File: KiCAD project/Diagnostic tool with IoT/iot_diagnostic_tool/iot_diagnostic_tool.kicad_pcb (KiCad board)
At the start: 4 copper layers, 50 x 50 mm, 113 parts, among them J2 USB, J3 693023010811, J5 Debug, J6 BOOT, J7 OBD, Q1 s8050, Q2 s8050, Q3 s8050, Q4 s8050, Q5 s8050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

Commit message: Update 07/03/23 - board layout done
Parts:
- removed D3, D4: LED, LED_SMD:LED_0402_1005Metric
- removed Q4, Q5: s8050, Package_TO_SOT_SMD:SOT-23
- removed R22, R26: 4k7, Resistor_SMD:R_0402_1005Metric
- removed R23, R27: 47k, Resistor_SMD:R_0402_1005Metric
- removed R24, R25: 2k2, Resistor_SMD:R_0402_1005Metric
- moved R14 32.0 mm to (147.0, 101.2)
- moved Q3 31.4 mm to (144.5, 100.4), turned to 0 degrees
- moved C25 31.1 mm to (142.1, 101.0)
- moved R15 29.9 mm to (145.1, 102.7), turned to 0 degrees
- moved R41 23.5 mm to (152.0, 83.9), turned to 180 degrees
- moved R43 22.3 mm to (144.8, 81.3), turned to 180 degrees
- moved R42 21.8 mm to (149.9, 83.9)
- moved Q7 18.7 mm to (150.8, 81.5), turned to 180 degrees
- moved Q6 16.0 mm to (147.7, 79.8)
- moved R40 13.8 mm to (150.9, 79.0), turned to 0 degrees
- moved R8 0.30 mm to (162.9, 99.3)
- moved R39 0.14 mm to (132.8, 77.8), turned to -90 degrees
- moved R38 0.08 mm to (140.6, 77.9), turned to -90 degrees
- moved D8 0.08 mm to (133.7, 117.7)
- turned R28 to 180 degrees
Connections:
- AE1 pad 1: Net-(AE1-A) -> ANT_MAIN
- AE1 pad 2: (no net) -> GND
- AE2 pad 1: Net-(AE2-A) -> ANT_GNSS
- AE2 pad 2: (no net) -> GND
- C1 pad 1: VDD -> +3V3
- C15 pad 1: VDD -> +3V3
- C16 pad 1: VDD -> +3V3
- C17 pad 1: VDD -> +3V3
- C18 pad 1: VDD -> +3V3
- C2 pad 1: VDD -> +3V3
- C21 pad 1: VBAT -> +3V3
- C22 pad 1: VBAT -> +3V3
- C23 pad 1: VBAT -> +3V3
- C24 pad 1: VBAT -> +3V3
- C28 pad 1: VDD -> +3V3
- C3 pad 1: VDD -> +3V3
- C39 pad 1: Net-(AE1-A) -> ANT_MAIN
- C4 pad 1: VDD -> +3V3
- C41 pad 1: Net-(AE2-A) -> ANT_GNSS
- C5 pad 1: VDD -> +3V3
- C6 pad 1: VDD -> +3V3
- C7 pad 1: VDD -> +3V3
- D11 pad 1: VBAT -> +3V3
- J2 pad 2: VDD -> +3V3
- J5 pad 1: VDD -> +3V3
- J6 pad 1: VDD -> +3V3
- L1 pad 2: VDD -> +3V3
- R12 pad 1: /car_comm/+12V_F -> /power_supply/+12V_F
- R16 pad 1: VBAT -> +3V3
- R2 pad 1: VDD -> +3V3
- R38 pad 2: Net-(AE1-A) -> ANT_MAIN
- R39 pad 2: Net-(AE2-A) -> ANT_GNSS
- R7 pad 1: /car_comm/+12V_F -> /power_supply/+12V_F
- R9 pad 1: /car_comm/+12V_F -> /power_supply/+12V_F
- U1 pad 1: VDD -> +3V3
- U1 pad 13: VDD -> +3V3
- U1 pad 19: VDD -> +3V3
- U1 pad 32: VDD -> +3V3
- U1 pad 48: VDD -> +3V3
- U1 pad 64: VDD -> +3V3
- U3 pad 3: VDD -> +3V3
- U4 pad 19: VBAT -> +3V3
- U4 pad 20: VBAT -> +3V3
- U4 pad 78: STATUS -> unconnected-(U4-STATUS-Pad78)
- U4 pad 79: NET_STATUS -> unconnected-(U4-NET_STATUS-Pad79)
- U6 pad 3: VDD -> +3V3
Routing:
- net NRST: track 9.75 -> 70.3 mm, vias 2 -> 0
- net +1V8: track 57.8 -> 97.7 mm
- net RESET_N: track 12.0 -> 45.9 mm, vias 2 -> 4
- net +3V3: track 0.00 -> 24.3 mm, vias 0 -> 22
- net VDD: track 21.0 -> 0.00 mm, vias 14 -> 0
- net IoT_PWR: track 1.48 -> 16.7 mm, vias 1 -> 2
- net GND: track 37.2 -> 22.2 mm, vias 57 -> 249
- net PON_TRIG: track 0.94 -> 12.2 mm
- net /power_supply/+12V_F: track 2.67 -> 11.3 mm, vias 0 -> 2
- net PON_TRIG_MCU: track 0.00 -> 7.67 mm, vias 0 -> 1
- net PWRKEY: track 5.71 -> 12.6 mm, vias 1 -> 0
- net ANT_MAIN: track 0.00 -> 6.68 mm
- net ANT_GNSS: track 0.00 -> 6.53 mm
- net Net-(Q6-G): track 0.00 -> 5.47 mm
- net Net-(Q3-B): track 0.00 -> 5.17 mm
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- added copper zone on F.Cu, net +3V3
- added copper zone on In2.Cu, net +3V3
- removed copper zone on F.Cu, net VBAT
- removed copper zone on F.Cu, net VDD

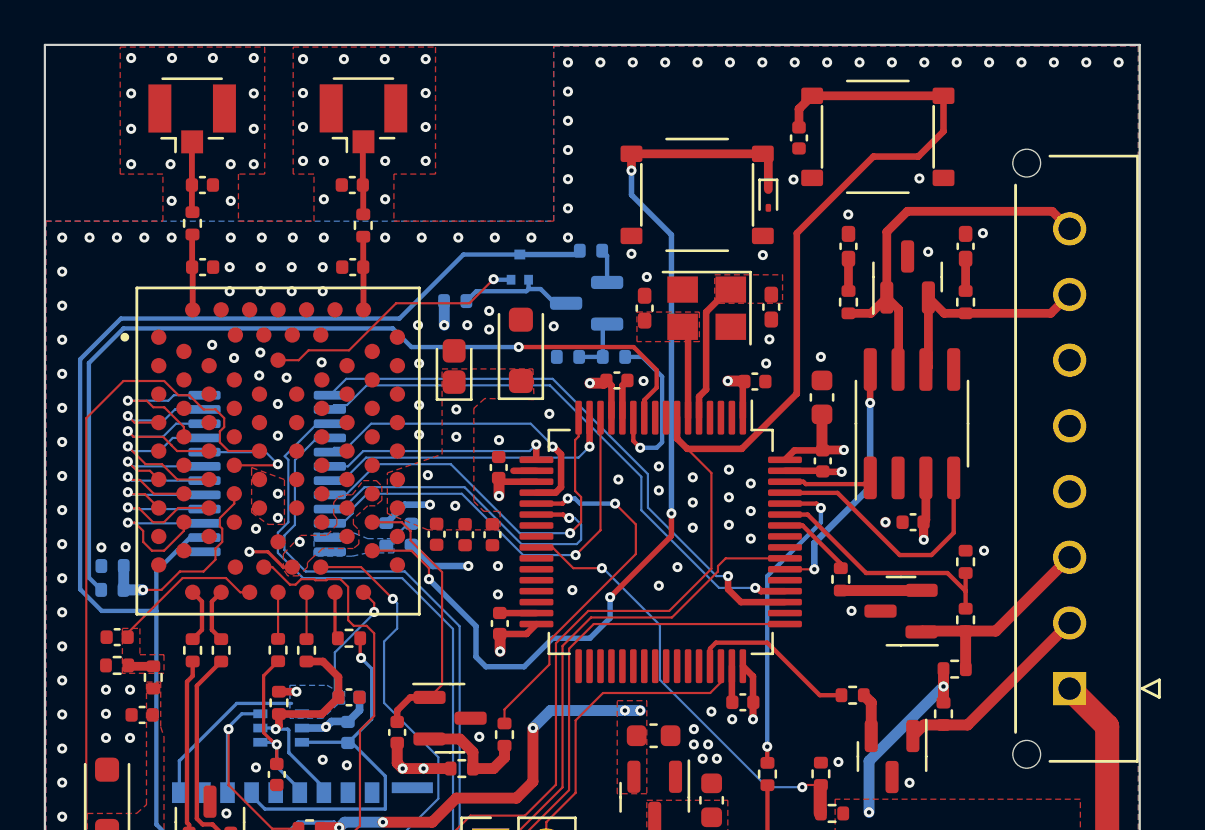
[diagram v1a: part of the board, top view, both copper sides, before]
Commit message: Update 13/03/23 - Board layout fixes
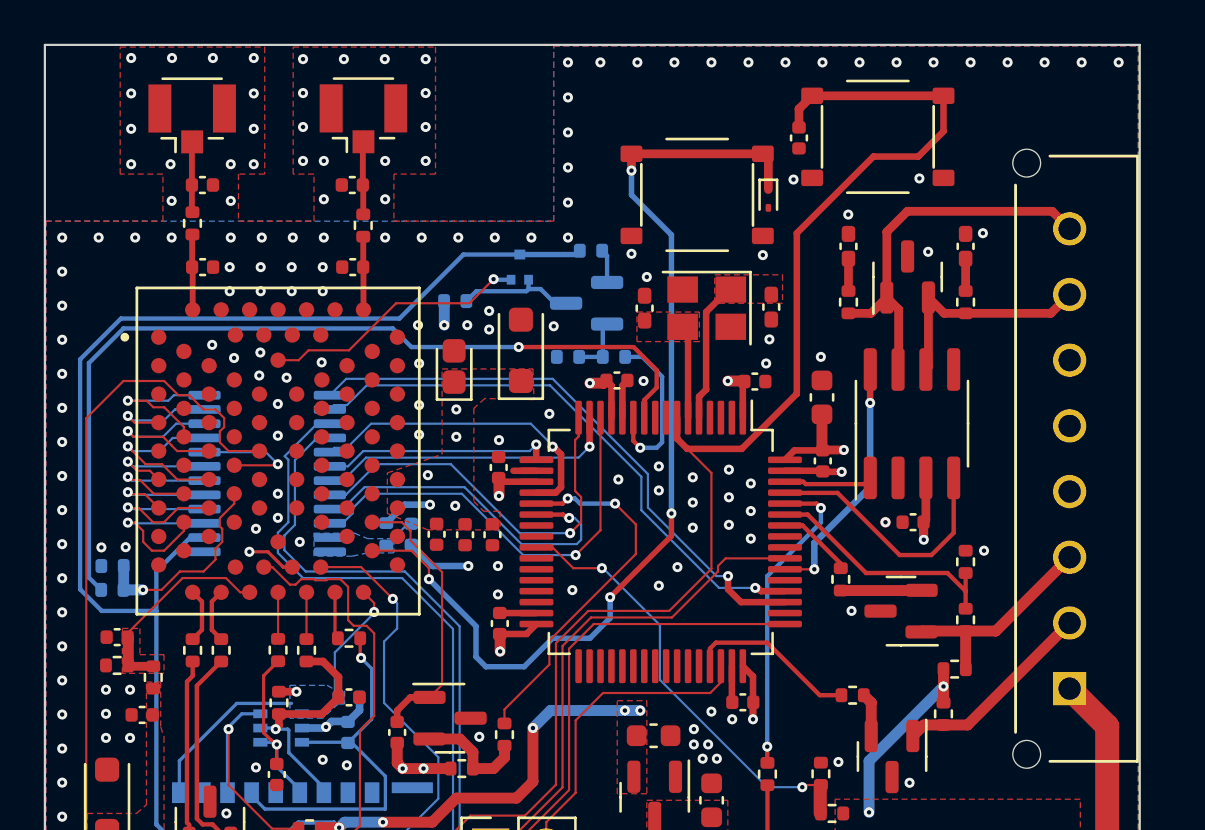
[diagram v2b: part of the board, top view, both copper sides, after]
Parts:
- turned R38 to 90 degrees
- turned R39 to 90 degrees
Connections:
- AE1 pad 1: ANT_MAIN -> /iot_module/antenna/ANT_M
- AE1 pad 2: GND -> (no net)
- AE2 pad 1: ANT_GNSS -> /iot_module/antenna/ANT_G
- AE2 pad 2: GND -> (no net)
- C33 pad 1: SIM_RST -> /iot_module/sim/SIM_RES
- C39 pad 1: ANT_MAIN -> /iot_module/antenna/ANT_M
- C41 pad 1: ANT_GNSS -> /iot_module/antenna/ANT_G
- D5 pad 3: SIM_RST -> /iot_module/sim/SIM_RES
- D7 pad 1: USB_D- -> USB_D-_5
- D7 pad 2: USB_D+ -> USB_D+_5
- J2 pad 3: USB_D+ -> USB_D+_5
- J2 pad 5: USB_D- -> USB_D-_5
- J3 pad C2: SIM_RST -> /iot_module/sim/SIM_RES
- R28 pad 1: SIM_RST -> /iot_module/sim/SIM_RES
- R35 pad 2: USB_D- -> USB_D-_5
- R36 pad 2: USB_D+ -> USB_D+_5
- R38 pad 2: ANT_MAIN -> /iot_module/antenna/ANT_M
- R39 pad 2: ANT_GNSS -> /iot_module/antenna/ANT_G
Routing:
- net SIM_RST: track 20.1 -> 2.15 mm, vias 1 -> 0
- net /iot_module/sim/SIM_RES: track 0.00 -> 17.9 mm, vias 0 -> 1
- net USB_D+_5: track 0.00 -> 14.0 mm
- net USB_D+: track 16.5 -> 2.49 mm
- net USB_D-_5: track 0.00 -> 13.4 mm
- net USB_D-: track 15.9 -> 2.49 mm
- net ANT_MAIN: track 6.68 -> 3.29 mm
- net /iot_module/antenna/ANT_M: track 0.00 -> 3.39 mm
- net /iot_module/antenna/ANT_G: track 0.00 -> 3.22 mm
- net ANT_GNSS: track 6.53 -> 3.31 mm
- net USB_VBUS: track 8.23 -> 9.53 mm
- net GND: vias 249 -> 245

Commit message: Update 17/03/23 - final board update, generated files for manufacturing
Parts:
- removed Q7: s8050, Package_TO_SOT_SMD:SOT-23
- added D2: LED, Diode_SMD:D_0603_1608Metric, F.Cu at (154.8, 72.0)
- added G***: LOGO, KiCAD project:vut_logo, F.Cu at (165.9, 104.2)
- added Q4: BC817, Package_TO_SOT_SMD:SOT-23, F.Cu at (164.4, 100.7)
- added Q5: BC817, Package_TO_SOT_SMD:SOT-23_Handsoldering, B.Cu at (155.8, 73.3)
- added R17: 2k2, Resistor_SMD:R_0402_1005Metric, F.Cu at (157.4, 73.3)
- added R18: 4k7, Resistor_SMD:R_0402_1005Metric, F.Cu at (151.2, 74.7)
- added R19: 47k, Resistor_SMD:R_0402_1005Metric, F.Cu at (151.7, 73.0)
- C24: footprint Capacitor_Tantalum_SMD:CP_EIA-1608-08_AVX-J -> Capacitor_Tantalum_SMD:CP_EIA-3528-21_Kemet-B
- C27, C32, C33, C34, C35: footprint Capacitor_SMD:C_0402_1005Metric -> Capacitor_SMD:C_0402_1005Metric_Pad0.74x0.62mm_HandSolder
- D5: footprint Package_TO_SOT_SMD:SOT-363_SC-70-6 -> Package_TO_SOT_SMD:SOT-363_SC-70-6_Handsoldering
- Q1, Q2: value s8050 -> BC817
- Q3: value s8050 -> BC817; footprint Package_TO_SOT_SMD:SOT-23 -> Package_TO_SOT_SMD:SOT-23_Handsoldering; moved to B.Cu
- R16, R40, R41, R42, R43, R44, R45: footprint Resistor_SMD:R_0402_1005Metric -> Resistor_SMD:R_0402_1005Metric_Pad0.72x0.64mm_HandSolder
- U6: footprint Package_TO_SOT_SMD:SOT-23 -> Package_TO_SOT_SMD:SOT-23_Handsoldering
- moved Q2 20.2 mm to (144.6, 100.5), turned to 180 degrees
- moved Q3 20.2 mm to (151.4, 81.5)
- moved J6 2.00 mm to (153.6, 110.6)
- moved R8 1.65 mm to (161.3, 99.8)
- moved Q1 1.04 mm to (164.6, 96.4), turned to 0 degrees
- moved R41 0.88 mm to (152.9, 83.9)
- moved C24 0.78 mm to (145.3, 84.8)
- moved C32 0.59 mm to (139.7, 98.9)
- moved R40 0.53 mm to (151.5, 79.0)
- moved R44 0.46 mm to (129.1, 95.0)
- moved U6 0.45 mm to (153.9, 104.5)
- moved D11 0.43 mm to (148.2, 83.7)
- moved R6 0.26 mm to (162.1, 94.1)
- moved C29 0.25 mm to (153.8, 101.0)
- moved R45 0.25 mm to (129.3, 93.3)
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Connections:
- Q1 pad 1: ISO_K -> Net-(Q1-B)
- Q1 pad 2: Net-(Q1-B) -> GND
- Q1 pad 3: GND -> ISO_K
- Q2 pad 1: ISO_L -> Net-(Q2-B)
- Q2 pad 2: Net-(Q2-B) -> GND
- Q2 pad 3: GND -> PWRKEY
- Q3 pad 1: PWRKEY -> Net-(Q3-B)
- Q3 pad 2: Net-(Q3-B) -> Net-(Q3-E)
- Q3 pad 3: GND -> Net-(Q3-C)
- Q6 pad 1: Net-(Q6-G) -> Net-(Q3-E)
- R14 pad 2: Net-(Q3-B) -> Net-(Q2-B)
- R15 pad 2: Net-(Q3-B) -> Net-(Q2-B)
- R28 pad 1: /iot_module/sim/SIM_RES -> SIM_RST
- R28 pad 2: SIM_RST -> /iot_module/sim/SIM_RES
- R37 pad 1: USB_BOOT_VCC -> +1V8
- R37 pad 2: +1V8 -> USB_BOOT_VCC
- R40 pad 2: Net-(Q7-C) -> Net-(Q3-C)
- R41 pad 2: Net-(Q7-B) -> Net-(Q3-B)
- R42 pad 1: Net-(Q7-B) -> Net-(Q3-B)
- R43 pad 1: Net-(Q6-G) -> Net-(Q3-E)
- R8 pad 1: Net-(Q2-B) -> Net-(Q4-B)
- U4 pad 79: unconnected-(U4-NET_STATUS-Pad79) -> NET_STATUS
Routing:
- net NET_STATUS: track 0.00 -> 26.3 mm
- net Net-(Q5-B): track 0.00 -> 7.58 mm, vias 0 -> 1
- net Net-(Q6-G): track 5.47 -> 0.00 mm
- net Net-(Q3-E): track 0.00 -> 5.39 mm
- net GND: track 22.2 -> 17.9 mm, vias 245 -> 256
- net Net-(Q5-C): track 0.00 -> 3.04 mm, vias 0 -> 1
- net Net-(Q3-C): track 0.00 -> 2.76 mm
- net Net-(Q7-B): track 2.66 -> 0.00 mm
- net Net-(D2-K): track 0.00 -> 2.38 mm
- net Net-(J6-Pin_2): track 9.98 -> 12.0 mm
- net +1V8: track 97.7 -> 99.5 mm
- net Net-(Q4-B): track 0.00 -> 1.70 mm
- net Net-(Q7-C): track 1.54 -> 0.00 mm
- net Net-(Q2-B): track 2.00 -> 3.47 mm
- net Net-(Q1-B): track 3.69 -> 2.23 mm
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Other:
- board text added: "+"
- board text added: "+ -"
- board text added: "+12"
- board text added: "BOOT"
- board text added: "BOOT0"
- board text added: "CAN H"
- board text added: "CAN L"
- board text added: "CLK"
- board text added: "D-RX"
- board text added: "D-TX"
- board text added: "GND"
- board text added: "GNSS"
- board text added: "IoT"
- board text added: "IoT RST"
- board text added: "JLCJLCJLCJLC"
- board text added: "K"
- board text added: "L"
- board text added: "MCU RST"
- board text added: "Miroslav Babeľa 2023"
- board text added: "NET"
- board text added: "NRST"
- board text added: "PHY"
- board text added: "SWDIO"
- board text added: "SWO"
- board text added: "VCC"
